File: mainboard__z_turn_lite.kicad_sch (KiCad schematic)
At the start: 5 parts

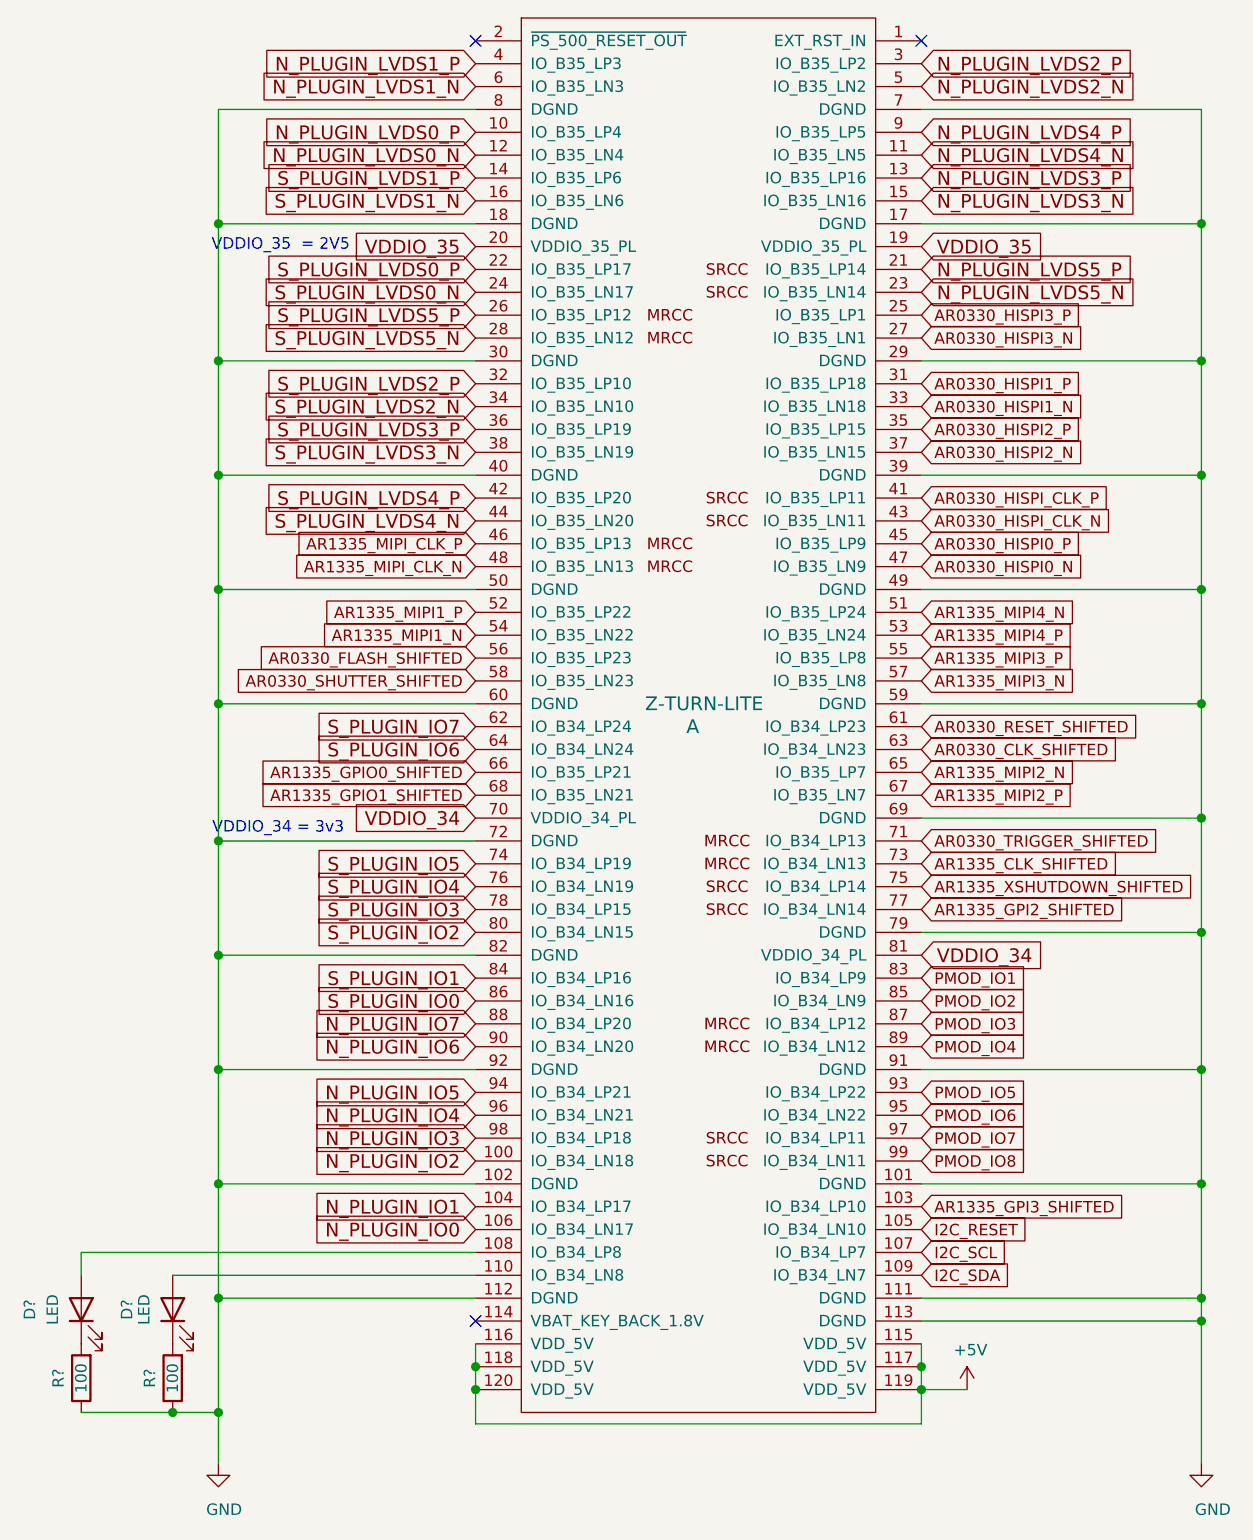
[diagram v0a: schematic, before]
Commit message: small tweaks; add mipi termination
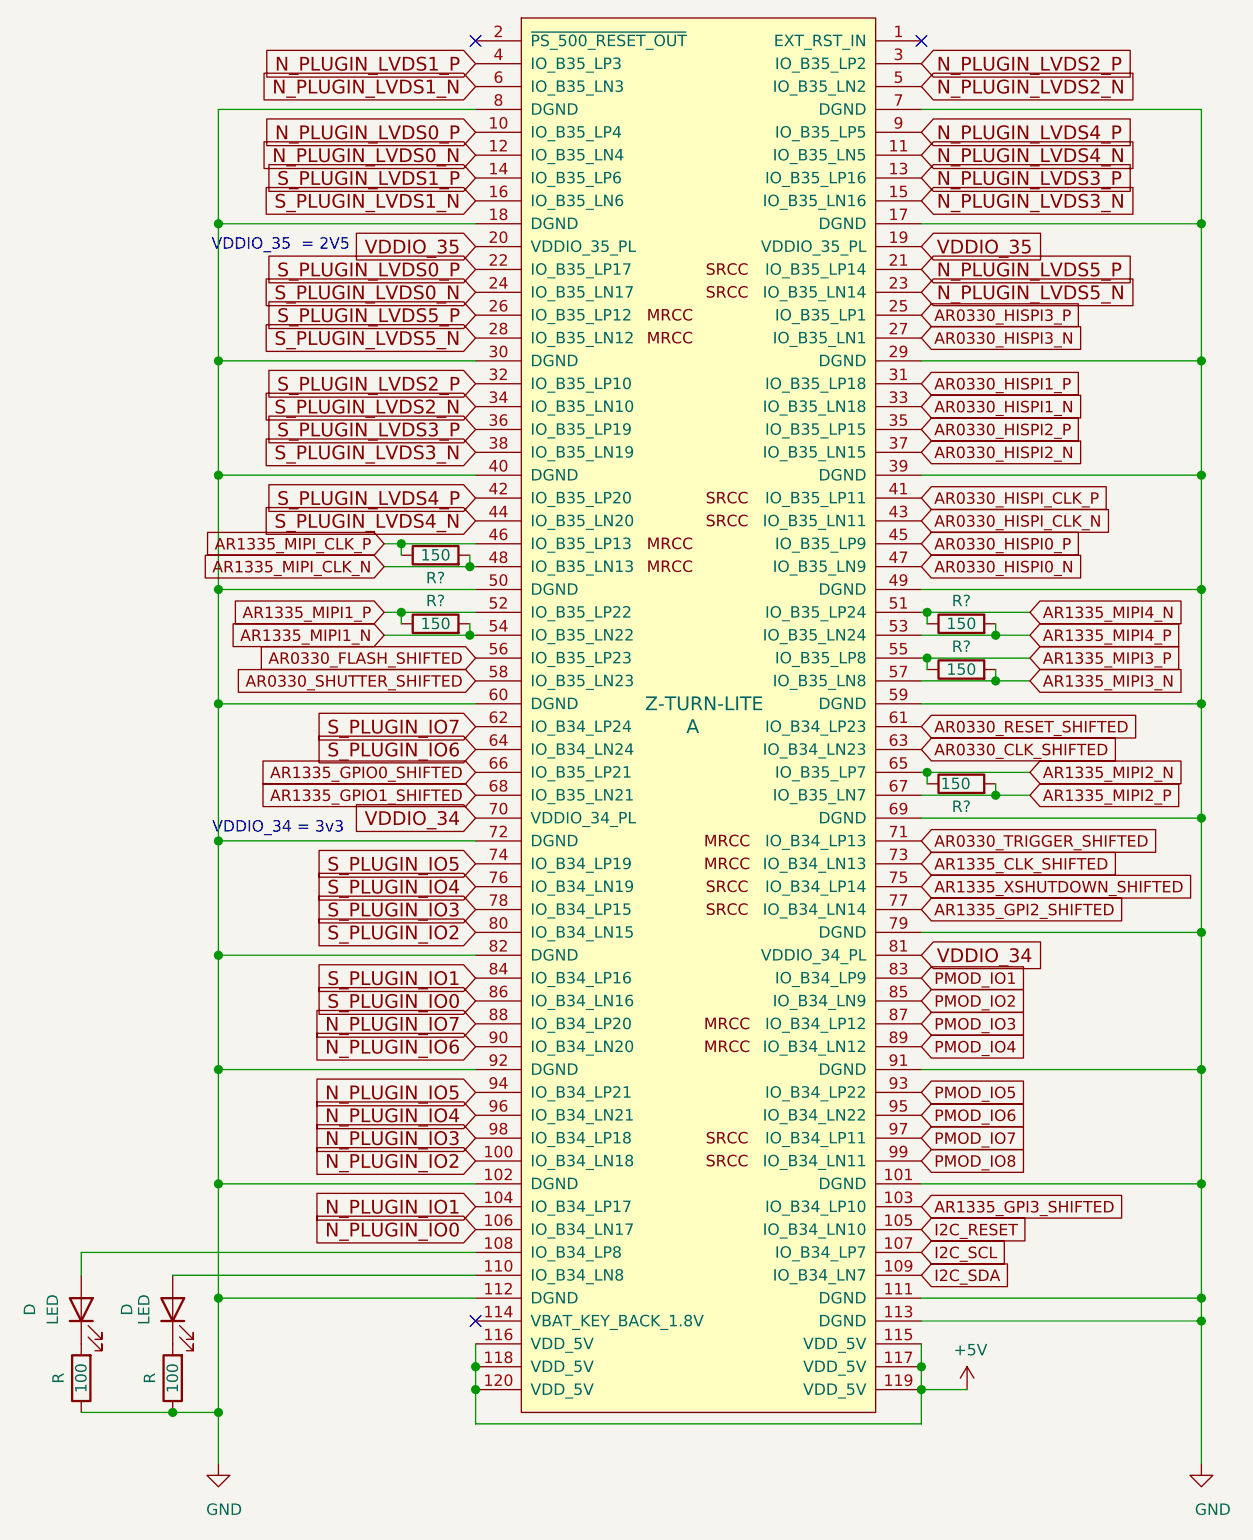
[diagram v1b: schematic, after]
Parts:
- added R? (x5): 150, symbol Device:R
- gave numbers to parts that had none: 2
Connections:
- net AR1335_MIPI1_N: now also R?.2
- net AR1335_MIPI1_P: now also R?.1
- net AR1335_MIPI2_N: now also R?.1
- net AR1335_MIPI2_P: now also R?.2
- net AR1335_MIPI3_N: now also R?.2
- net AR1335_MIPI3_P: now also R?.1
- net AR1335_MIPI4_N: now also R?.1
- net AR1335_MIPI4_P: now also R?.2
- net AR1335_MIPI_CLK_N: now also R?.2
- net AR1335_MIPI_CLK_P: now also R?.1
